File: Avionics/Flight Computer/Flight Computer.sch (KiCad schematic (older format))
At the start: 13 parts

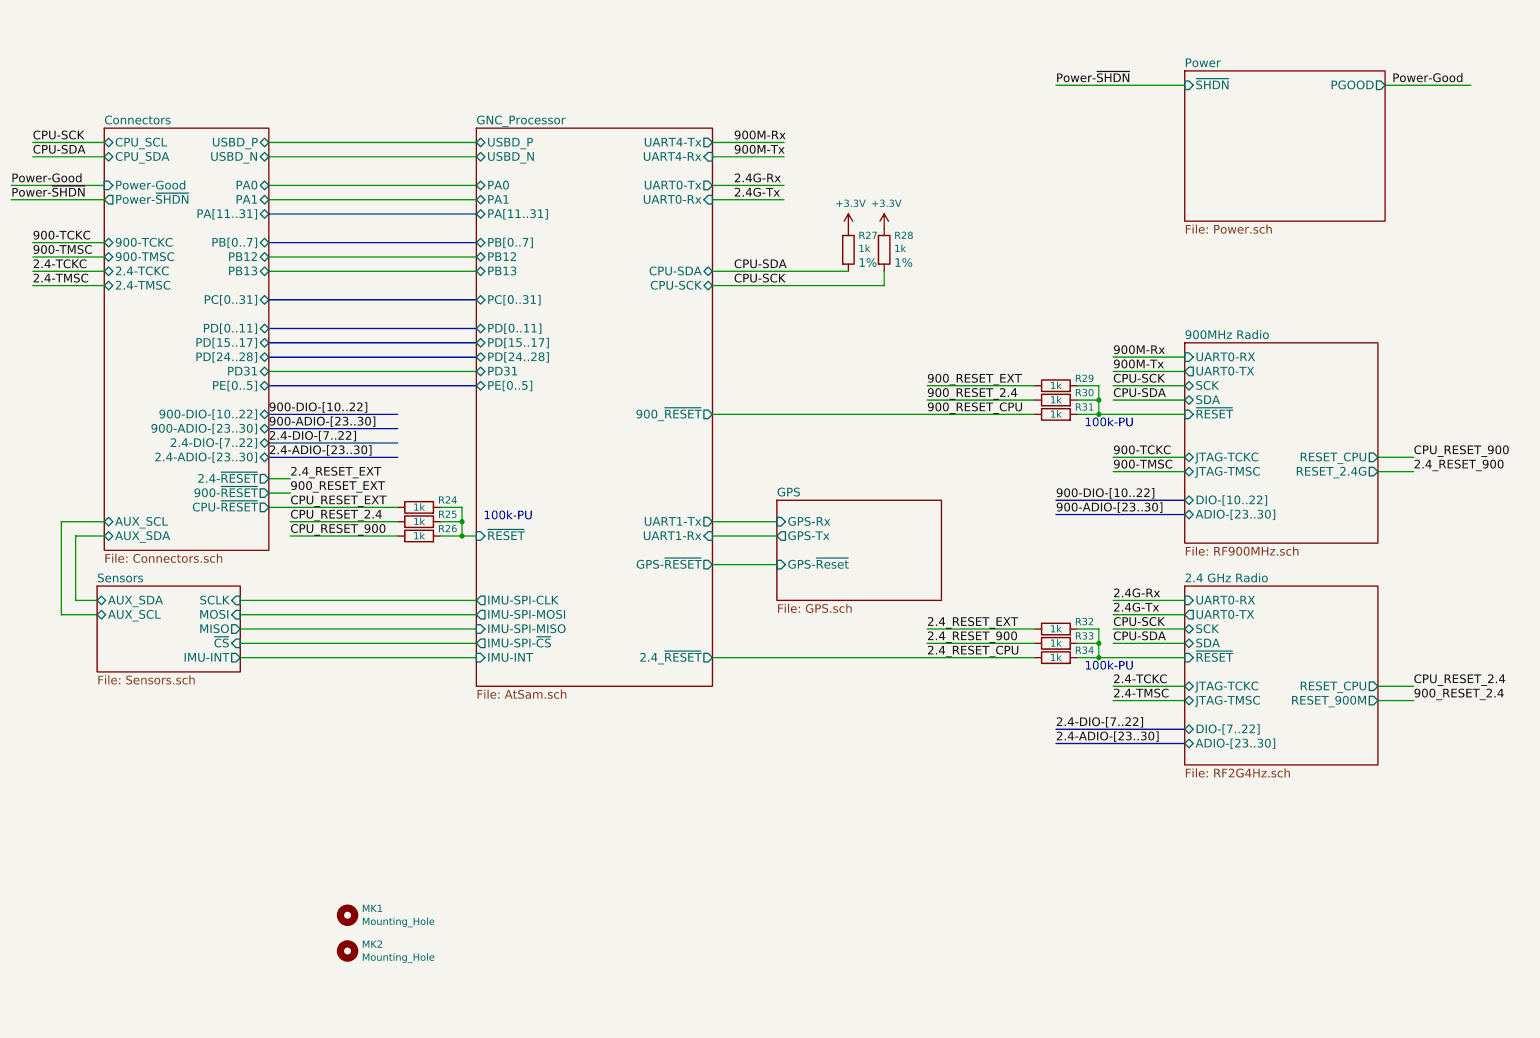
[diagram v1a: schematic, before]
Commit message: Added LEDs
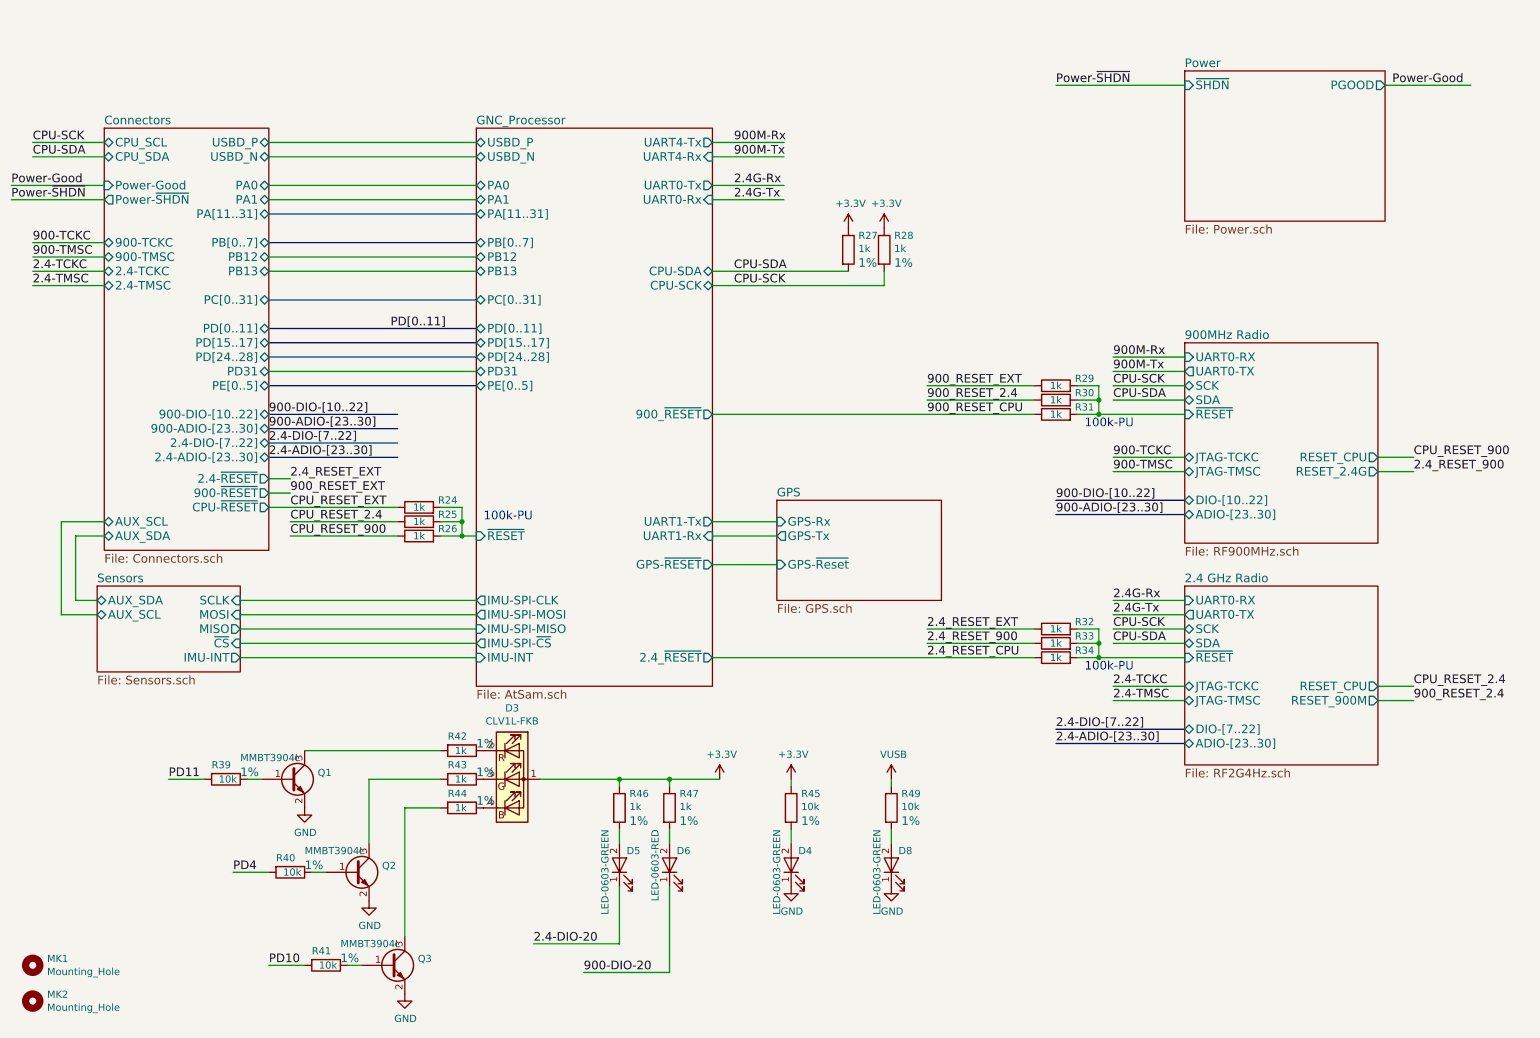
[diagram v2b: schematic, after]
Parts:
- added D3: CLV1L-FKB, LEDs:LED_Cree-PLCC4_3.2x2.8mm, symbol LED_ARGB
- added D4, D5, D8: LED-0603-GREEN, LEDs:LED_0603, symbol LED
- added D6: LED-0603-RED, LEDs:LED_0603, symbol LED
- added Q1, Q2, Q3: MMBT3904L, TO_SOT_Packages_SMD:SOT-23, symbol Q_NPN_BEC
- added R39, R40, R41, R45, R49: 10k, Resistors_SMD:R_0402, symbol R
- added R42, R43, R44, R46, R47: 1k, Resistors_SMD:R_0402, symbol R
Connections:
- net labels added: 2.4-DIO-20, 900-DIO-20, GND, PD10, PD11, PD4, PD[0..11], VUSB
- wire segments 77 -> 101
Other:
- moved on the sheet: MK1, MK2

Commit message: Changed LED configuration, added smart driver chip to let all the CPUs access it..
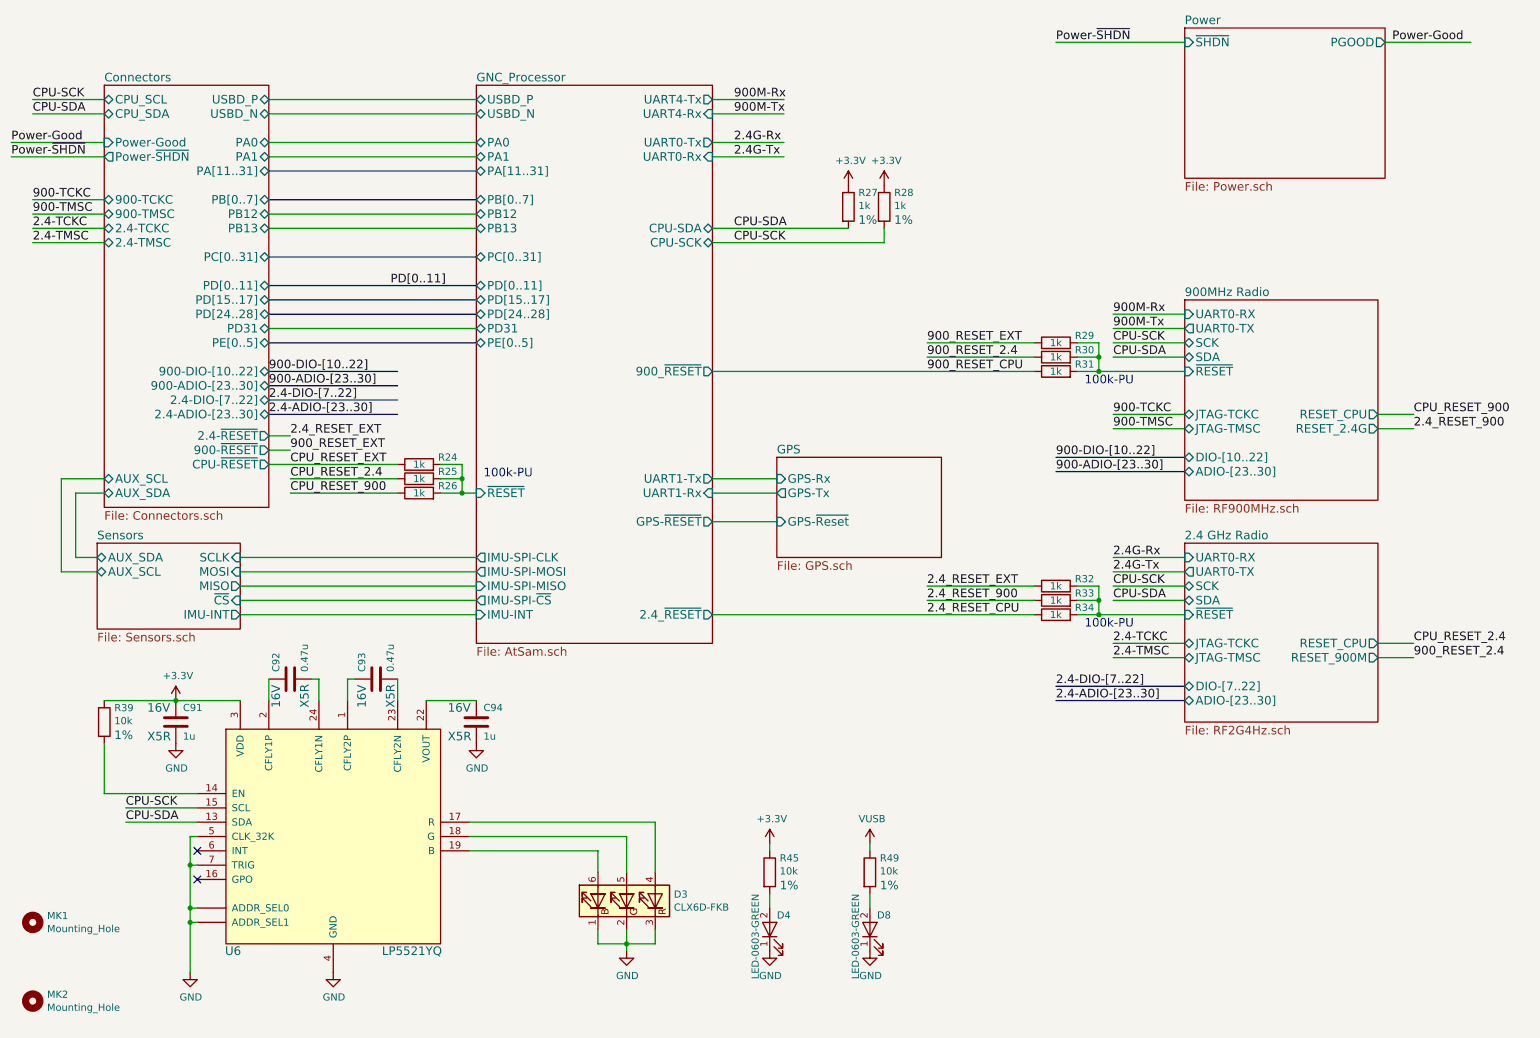
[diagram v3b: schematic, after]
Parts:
- removed D3: CLV1L-FKB, LEDs:LED_Cree-PLCC4_3.2x2.8mm, symbol LED_ARGB
- removed D5: LED-0603-GREEN, LEDs:LED_0603, symbol LED
- removed D6: LED-0603-RED, LEDs:LED_0603, symbol LED
- removed Q1, Q2, Q3: MMBT3904L, TO_SOT_Packages_SMD:SOT-23, symbol Q_NPN_BEC
- removed R40, R41: 10k, Resistors_SMD:R_0402, symbol R
- removed R42, R43, R44, R46, R47: 1k, Resistors_SMD:R_0402, symbol R
- added C91, C94: 1u, Capacitors_SMD:C_0402, symbol C
- added C92, C93: 0.47u, Capacitors_SMD:C_0402, symbol C
- added D3: CLX6D-FKB, LEDs:LED_PLCC6_3.4x3.4mm, symbol LED_BGR
- added U6: LP5521YQ, Housings_DFN_QFN:QFN-24-1EP_4x5mm_Pitch0.5mm, symbol LP5521YQ
- R24, R25, R26, R27, R28, R29, R30, R31, R32, R33, R34, R39, R45, R49: Voltage 50V -> 16V
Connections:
- net labels removed: 2.4-DIO-20, 900-DIO-20, PD10, PD11, PD4
- wire segments 101 -> 108
- no-connect marks 0 -> 2
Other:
- moved on the sheet: D4, D8, MK1, R24, R25, R26, R27, R28, R29, R30, R31, R32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

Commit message: DFM/BOM Optimizations
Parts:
- D3: Manufacturer Part Number (none) -> CLX6D-FKB-CMPQSGKBB7A363
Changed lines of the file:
@@
 F 2 "LEDs:LED_PLCC6_3.4x3.4mm" H 200 150 50  0001 C CNN
 F 3 "http://www.cree.com/~/media/Files/Cree/LED-Components-and-Modules/HB/Data-Sheets/1278-CLX6D-FKB.pdf" H 200 150 50  0001 C CNN
+F 4 "CLX6D-FKB-CMPQSGKBB7A363" V 4850 6900 60  0001 C CNN "Manufacturer Part Number"
 	1    4850 6900
 	0    -1   -1   0

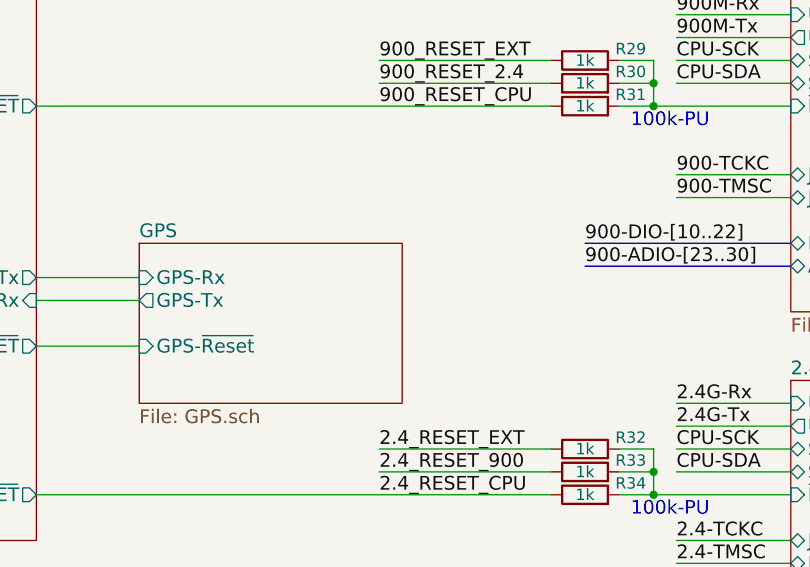
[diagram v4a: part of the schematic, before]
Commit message: Added Logo, connected GPS SDA/SCL, and cleaned silk.
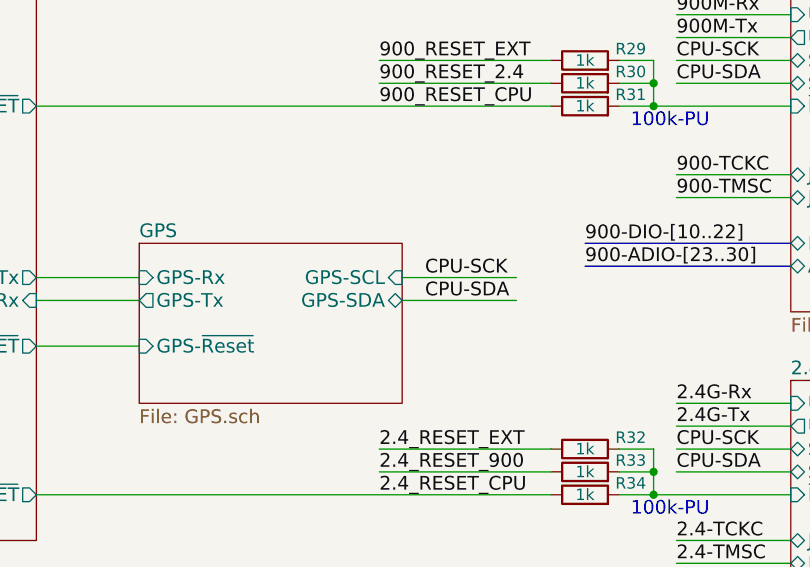
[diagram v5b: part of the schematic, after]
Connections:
- wire segments 108 -> 110
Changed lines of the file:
@@
 F3 "GPS-Tx" O L 5900 4050 60
 F4 "GPS-~Reset" I L 5900 4250 60
+F5 "GPS-SCL" I R 7050 3950 60
+F6 "GPS-SDA" B R 7050 4050 60
 $EndSheet
 $Sheet
@@
 Wire Wire Line
 	5050 6350 5050 6700
+Text Label 7150 3950 0    60   ~ 0
+CPU-SCK
+Text Label 7150 4050 0    60   ~ 0
+CPU-SDA
+Wire Wire Line
+	7050 3950 7550 3950
+Wire Wire Line
+	7050 4050 7550 4050
 $EndSCHEMATC
